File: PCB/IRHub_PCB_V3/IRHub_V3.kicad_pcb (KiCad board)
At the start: 2 copper layers, 80 x 80 mm, 85 parts, among them Q1 UMH3N, SW1 SW_Push, U1 DRV2605LDGS

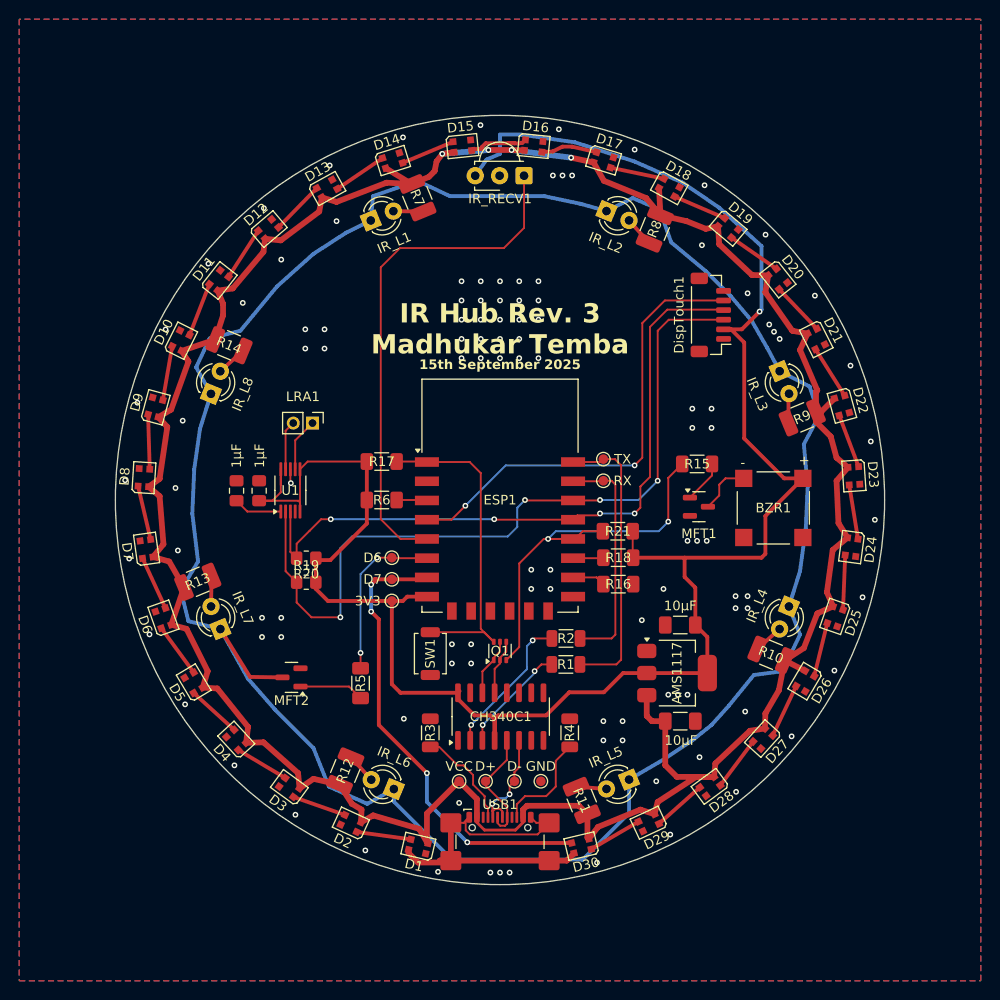
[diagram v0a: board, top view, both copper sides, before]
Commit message: fix pcb led issue :)
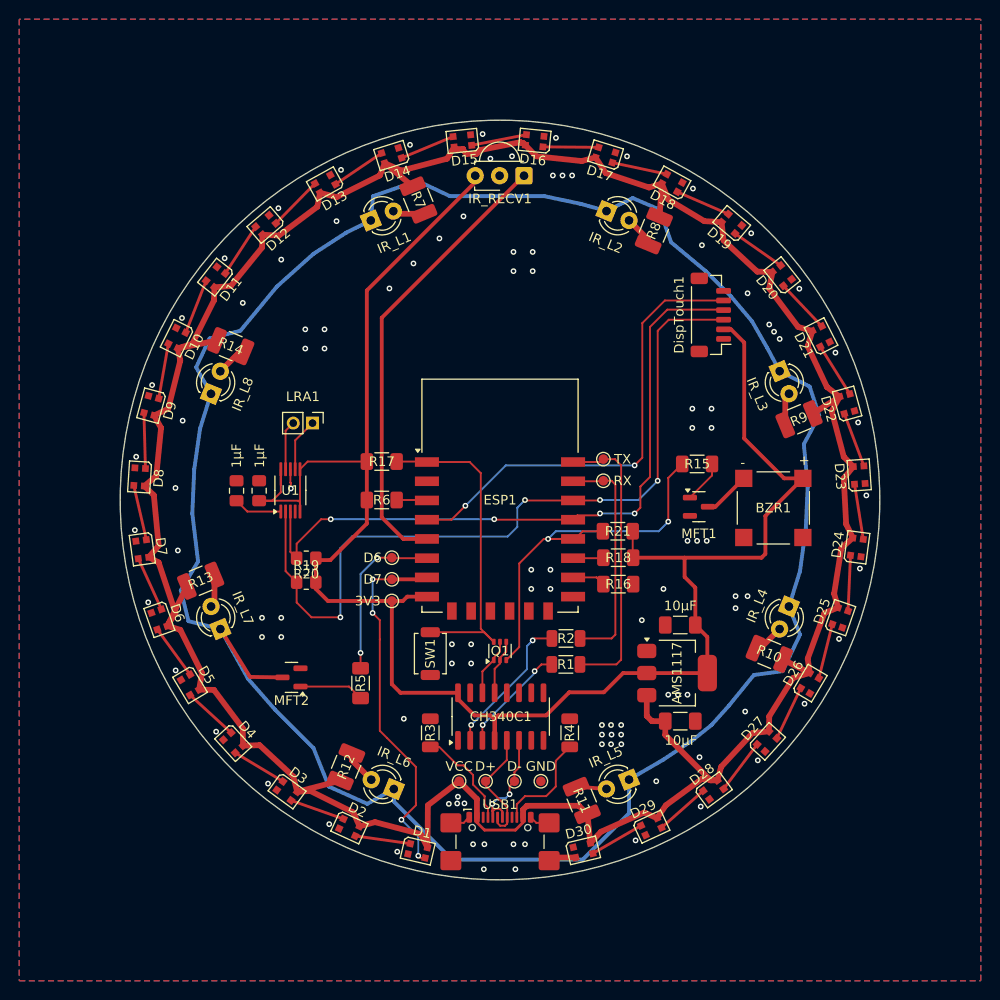
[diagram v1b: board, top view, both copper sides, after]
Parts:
- moved D20 0.57 mm to (179.3, 76.7), turned to 128.4 degrees
- moved D21 0.57 mm to (183.4, 83.0), turned to 116.9 degrees
- moved D19 0.57 mm to (174.1, 71.3), turned to 139.9 degrees
- moved D22 0.56 mm to (186.1, 90.0), turned to 105.4 degrees
- moved D18 0.56 mm to (167.9, 67.0), turned to 151.4 degrees
- moved D23 0.56 mm to (187.4, 97.4), turned to 93.9 degrees
- moved D17 0.56 mm to (161.0, 64.1), turned to 162.9 degrees
- moved D24 0.55 mm to (187.1, 104.9), turned to 82.4 degrees
- moved D16 0.55 mm to (153.6, 62.6), turned to 174.4 degrees
- moved D25 0.54 mm to (185.4, 112.2), turned to 70.9 degrees
- moved D15 0.54 mm to (146.1, 62.7), turned to -174.1 degrees
- moved D26 0.53 mm to (182.2, 119.0), turned to 59.4 degrees
- moved D14 0.53 mm to (138.7, 64.2), turned to -162.6 degrees
- moved D27 0.52 mm to (177.8, 125.1), turned to 47.9 degrees
- moved D13 0.52 mm to (131.8, 67.1), turned to -151.1 degrees
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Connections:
- D1 pad 1: unconnected-(D1-DOUT-Pad1) -> Net-(D1-DOUT)
- D1 pad 2: +5V -> GND
- D1 pad 3: Net-(D1-DIN) -> D7
- D1 pad 4: GND -> +5V
- D10 pad 2: +5V -> GND
- D10 pad 4: GND -> +5V
- D11 pad 1: Net-(D10-DIN) -> Net-(D11-DOUT)
- D11 pad 2: +5V -> GND
- D11 pad 3: Net-(D11-DIN) -> Net-(D10-DOUT)
- D11 pad 4: GND -> +5V
- D12 pad 1: Net-(D11-DIN) -> Net-(D12-DOUT)
- D12 pad 2: +5V -> GND
- D12 pad 3: Net-(D12-DIN) -> Net-(D11-DOUT)
- D12 pad 4: GND -> +5V
- D13 pad 1: Net-(D12-DIN) -> Net-(D13-DOUT)
- D13 pad 2: +5V -> GND
- D13 pad 3: Net-(D13-DIN) -> Net-(D12-DOUT)
- D13 pad 4: GND -> +5V
- D14 pad 1: Net-(D13-DIN) -> Net-(D14-DOUT)
- D14 pad 2: +5V -> GND
- D14 pad 3: Net-(D14-DIN) -> Net-(D13-DOUT)
- D14 pad 4: GND -> +5V
- D15 pad 1: Net-(D14-DIN) -> Net-(D15-DOUT)
- D15 pad 2: +5V -> GND
- D15 pad 3: Net-(D15-DIN) -> Net-(D14-DOUT)
- D15 pad 4: GND -> +5V
- D16 pad 1: Net-(D15-DIN) -> Net-(D16-DOUT)
- D16 pad 2: +5V -> GND
- D16 pad 3: Net-(D16-DIN) -> Net-(D15-DOUT)
- D16 pad 4: GND -> +5V
- D17 pad 1: Net-(D16-DIN) -> Net-(D17-DOUT)
- D17 pad 2: +5V -> GND
- D17 pad 3: Net-(D17-DIN) -> Net-(D16-DOUT)
- D17 pad 4: GND -> +5V
- D18 pad 1: Net-(D17-DIN) -> Net-(D18-DOUT)
- D18 pad 2: +5V -> GND
- D18 pad 3: Net-(D18-DIN) -> Net-(D17-DOUT)
- D18 pad 4: GND -> +5V
- D19 pad 1: Net-(D18-DIN) -> Net-(D19-DOUT)
- D19 pad 2: +5V -> GND
- D19 pad 3: Net-(D19-DIN) -> Net-(D18-DOUT)
- D19 pad 4: GND -> +5V
- D2 pad 1: Net-(D1-DIN) -> Net-(D2-DOUT)
- D2 pad 2: +5V -> GND
- D2 pad 3: Net-(D2-DIN) -> Net-(D1-DOUT)
- D2 pad 4: GND -> +5V
- D20 pad 1: Net-(D19-DIN) -> Net-(D20-DOUT)
- D20 pad 2: +5V -> GND
- D20 pad 3: Net-(D20-DIN) -> Net-(D19-DOUT)
- D20 pad 4: GND -> +5V
- D21 pad 1: Net-(D20-DIN) -> Net-(D21-DOUT)
- D21 pad 2: +5V -> GND
- D21 pad 3: Net-(D21-DIN) -> Net-(D20-DOUT)
- D21 pad 4: GND -> +5V
- D22 pad 1: Net-(D21-DIN) -> Net-(D22-DOUT)
- D22 pad 2: +5V -> GND
- D22 pad 3: Net-(D22-DIN) -> Net-(D21-DOUT)
- D22 pad 4: GND -> +5V
- D23 pad 1: Net-(D22-DIN) -> Net-(D23-DOUT)
- D23 pad 2: +5V -> GND
- D23 pad 3: Net-(D23-DIN) -> Net-(D22-DOUT)
- D23 pad 4: GND -> +5V
- D24 pad 1: Net-(D23-DIN) -> Net-(D24-DOUT)
- D24 pad 2: +5V -> GND
- D24 pad 3: Net-(D24-DIN) -> Net-(D23-DOUT)
- D24 pad 4: GND -> +5V
- D25 pad 1: Net-(D24-DIN) -> Net-(D25-DOUT)
- D25 pad 2: +5V -> GND
- D25 pad 3: Net-(D25-DIN) -> Net-(D24-DOUT)
- D25 pad 4: GND -> +5V
- D26 pad 1: Net-(D25-DIN) -> Net-(D26-DOUT)
- D26 pad 2: +5V -> GND
- D26 pad 3: Net-(D26-DIN) -> Net-(D25-DOUT)
- D26 pad 4: GND -> +5V
- D27 pad 1: Net-(D26-DIN) -> Net-(D27-DOUT)
- D27 pad 2: +5V -> GND
- D27 pad 3: Net-(D27-DIN) -> Net-(D26-DOUT)
- D27 pad 4: GND -> +5V
- D28 pad 1: Net-(D27-DIN) -> Net-(D28-DOUT)
- D28 pad 2: +5V -> GND
- D28 pad 3: Net-(D28-DIN) -> Net-(D27-DOUT)
- D28 pad 4: GND -> +5V
- D29 pad 1: Net-(D28-DIN) -> Net-(D29-DOUT)
- D29 pad 2: +5V -> GND
- D29 pad 3: Net-(D29-DIN) -> Net-(D28-DOUT)
- D29 pad 4: GND -> +5V
- D3 pad 1: Net-(D2-DIN) -> Net-(D3-DOUT)
- D3 pad 2: +5V -> GND
- D3 pad 3: Net-(D3-DIN) -> Net-(D2-DOUT)
- D3 pad 4: GND -> +5V
- D30 pad 1: Net-(D29-DIN) -> unconnected-(D30-DOUT-Pad1)
- D30 pad 2: +5V -> GND
- D30 pad 3: D7 -> Net-(D29-DOUT)
- D30 pad 4: GND -> +5V
- D4 pad 1: Net-(D3-DIN) -> Net-(D4-DOUT)
- D4 pad 2: +5V -> GND
- D4 pad 3: Net-(D4-DIN) -> Net-(D3-DOUT)
- D4 pad 4: GND -> +5V
- D5 pad 1: Net-(D4-DIN) -> Net-(D5-DOUT)
- D5 pad 2: +5V -> GND
- D5 pad 3: Net-(D5-DIN) -> Net-(D4-DOUT)
- D5 pad 4: GND -> +5V
- D6 pad 1: Net-(D5-DIN) -> Net-(D6-DOUT)
- D6 pad 2: +5V -> GND
- D6 pad 3: Net-(D6-DIN) -> Net-(D5-DOUT)
- D6 pad 4: GND -> +5V
- D7 pad 1: Net-(D6-DIN) -> Net-(D7-DOUT)
- D7 pad 2: +5V -> GND
- D7 pad 3: Net-(D7-DIN) -> Net-(D6-DOUT)
- D7 pad 4: GND -> +5V
- D8 pad 1: Net-(D7-DIN) -> Net-(D8-DOUT)
- D8 pad 2: +5V -> GND
- D8 pad 3: Net-(D8-DIN) -> Net-(D7-DOUT)
- D8 pad 4: GND -> +5V
- D9 pad 1: Net-(D8-DIN) -> Net-(D10-DIN)
- D9 pad 2: +5V -> GND
- D9 pad 3: Net-(D10-DOUT) -> Net-(D8-DOUT)
- D9 pad 4: GND -> +5V
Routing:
- net GND: track 41.2 -> 10.0 mm, vias 113 -> 108
- net +3.3V: track 209.8 -> 195.9 mm, vias 1 -> 0
- net +5V: track 292.0 -> 305.5 mm, vias 4 -> 0
- net D7: track 48.1 -> 38.5 mm
- net D5: track 53.9 -> 47.3 mm
- net Net-(D15-DIN): track 6.18 -> 0.00 mm
- net Net-(D16-DIN): track 5.89 -> 0.00 mm
- net Net-(D6-DOUT): track 0.00 -> 5.80 mm
- net Net-(D28-DOUT): track 0.00 -> 5.80 mm
- net Net-(D23-DOUT): track 0.00 -> 5.80 mm
- net Net-(D17-DOUT): track 0.00 -> 5.80 mm
- net Net-(D1-DOUT): track 0.00 -> 5.80 mm
- net Net-(D7-DOUT): track 0.00 -> 5.80 mm
- net Net-(D4-DOUT): track 0.00 -> 5.80 mm
- net Net-(D27-DOUT): track 0.00 -> 5.80 mm
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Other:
- board size 80 x 80 mm -> 79 x 79 mm
- board text removed: "15th September 2025"
- board text removed: "IR Hub Rev. 3 Madhukar Temba"

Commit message: new pcb
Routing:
- net D7: track 38.5 -> 39.2 mm
- net D6: track 17.4 -> 18.1 mm
- net GND: vias 108 -> 112
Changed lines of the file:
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@@
 	)
 	(via
+		(at 153.2 77.2)
+		(size 0.6)
+		(drill 0.3)
+		(layers "F.Cu" "B.Cu")
+		(free yes)
+		(net 2)
+	)
+	(via
 		(at 140 122.75)
 		(size 0.6)
@@
 	)
 	(via
-		(at 151.4 74.2)
+		(at 147.2 77.2)
+		(size 0.6)
+		(drill 0.3)
+		(layers "F.Cu" "B.Cu")
+		(free yes)
+		(net 2)
+	)
+	(via
+		(at 151.2 77.2)
 		(size 0.6)
 		(drill 0.3)
@@
 	)
 	(via
-		(at 151.4 76.2)
+		(at 147.2 79.2)
 		(size 0.6)
 		(drill 0.3)
@@
 	)
 	(via
+		(at 153.2 79.2)
+		(size 0.6)
+		(drill 0.3)
+		(layers "F.Cu" "B.Cu")
+		(free yes)
+		(net 2)
+	)
+	(via
 		(at 149 64.5)
 		(size 0.6)
@@
 	)
 	(via
-		(at 153.4 74.2)
+		(at 149.2 77.2)
 		(size 0.6)
 		(drill 0.3)
@@
 	)
 	(via
-		(at 153.4 76.2)
+		(at 149.2 79.2)
 		(size 0.6)
 		(drill 0.3)
@@
 	)
 	(via
+		(at 151.2 79.2)
+		(size 0.6)
+		(drill 0.3)
+		(layers "F.Cu" "B.Cu")
+		(free yes)
+		(net 2)
+	)
+	(via
 		(at 155.5 66.25)
 		(size 0.6)
@@
 	)
 	(segment
-		(start 141.726358 137.226358)
-		(end 141.5 137)
-		(width 0.2)
+		(start 141.2 131)
+		(end 141.2 127.8)
+		(width 0.4)
 		(layer "F.Cu")
 		(net 47)
 	)
 	(segment
-		(start 137.5 124)
-		(end 137.5 114.5)
-		(width 0.2)
+		(start 141.5 136.5)
+		(end 141.586019 136.586019)
+		(width 0.4)
 		(layer "F.Cu")
 		(net 47)
 	)
 	(segment
-		(start 141.25 131.5)
-		(end 141.25 127.75)
-		(width 0.2)
+		(start 141.586019 136.586019)
+		(end 141.586019 136.6)
+		(width 0.4)
 		(layer "F.Cu")
 		(net 47)
 	)
 	(segment
-		(start 139.75 133.25)
-		(end 141.25 131.75)
-		(width 0.2)
+		(start 141.586019 136.6)
+		(end 142.212377 137.226358)
+		(width 0.4)
 		(layer "F.Cu")
 		(net 47)
 	)
 	(segment
-		(start 136.75 108.25)
-		(end 138.75 108.25)
-		(width 0.2)
+		(start 138.75 108.25)
+		(end 136.75 108.25)
+		(width 0.4)
 		(layer "F.Cu")
 		(net 47)
@@
 	)
 	(segment
-		(start 138.25 124.75)
-		(end 137.5 124)
-		(width 0.2)
-		(layer "F.Cu")
-		(net 47)
-	)
-	(segment
-		(start 141.25 127.75)
-		(end 138.25 124.75)
-		(width 0.2)
+		(start 139.1 133.1)
+		(end 141.2 131)
+		(width 0.4)
 		(layer "F.Cu")
 		(net 47)
 	)
 	(segment
-		(start 141.25 131.75)
-		(end 141.25 131.5)
-		(width 0.2)
+		(start 137.4 112.4)
+		(end 136.8 111.8)
+		(width 0.4)
 		(layer "F.Cu")
 		(net 47)
 	)
 	(segment
-		(start 142.212377 137.226358)
-		(end 141.726358 137.226358)
-		(width 0.2)
+		(start 141.2 127.8)
+		(end 137.4 124)
+		(width 0.4)
 		(layer "F.Cu")
 		(net 47)
 	)
 	(segment
-		(start 137.5 112.5)
-		(end 136.75 111.75)
-		(width 0.2)
+		(start 136.75 108.25)
+		(end 136.6 108.4)
+		(width 0.4)
 		(layer "F.Cu")
 		(net 47)
 	)
 	(segment
-		(start 137.5 114.5)
-		(end 137.5 112.5)
-		(width 0.2)
+		(start 138.75 108.25)
+		(end 142.2 108.25)
+		(width 0.4)
 		(layer "F.Cu")
 		(net 47)
 	)
 	(segment
-		(start 138.75 108.25)
-		(end 142.2 108.25)
+		(start 137.4 124)
+		(end 137.4 112.4)
 		(width 0.4)
 		(layer "F.Cu")
@@
 	)
 	(via
-		(at 136.75 108.25)
+		(at 141.5 136.5)
 		(size 0.6)
 		(drill 0.3)
@@
 	)
 	(via
-		(at 141.5 137)
+		(at 136.8 111.8)
 		(size 0.6)
 		(drill 0.3)
@@
 	)
 	(via
-		(at 136.75 111.75)
+		(at 136.6 108.4)
 		(size 0.6)
 		(drill 0.3)
@@
 	)
 	(via
-		(at 139.75 133.25)
+		(at 139.1 133.1)
 		(size 0.6)
 		(drill 0.3)
@@
 	)
 	(segment
-		(start 141.5 137)
-		(end 141.5 135)
-		(width 0.2)
+		(start 139.1 133.1)
+		(end 139.4 133.4)
+		(width 0.4)
 		(layer "B.Cu")
 		(net 47)
 	)
 	(segment
-		(start 141.5 135)
-		(end 139.75 133.25)
-		(width 0.2)
+		(start 140 133.4)
+		(end 141.4 134.8)
+		(width 0.4)
 		(layer "B.Cu")
 		(net 47)
 	)
 	(segment
-		(start 136.75 111.75)
-		(end 136.75 108.25)
-		(width 0.2)
+		(start 141.4 136.4)
+		(end 141.5 136.5)
+		(width 0.4)
+		(layer "B.Cu")
+		(net 47)
+	)
+	(segment
+		(start 141.4 134.8)
+		(end 141.4 136.4)
+		(width 0.4)
+		(layer "B.Cu")
+		(net 47)
+	)
+	(segment
+		(start 136.6 108.4)
+		(end 136.6 111.6)
+		(width 0.4)
+		(layer "B.Cu")
+		(net 47)
+	)
+	(segment
+		(start 136.6 111.6)
+		(end 136.8 111.8)
+		(width 0.4)
+		(layer "B.Cu")
+		(net 47)
+	)
+	(segment
+		(start 139.4 133.4)
+		(end 140 133.4)
+		(width 0.4)
 		(layer "B.Cu")
 		(net 47)
@@
 		(start 142.4 106.05)
 		(end 138.8 106.05)
-		(width 0.2)
+		(width 0.4)
 		(layer "F.Cu")
 		(net 55)
 	)
 	(segment
-		(start 135.5 115.9)
-		(end 135.5 117.5)
-		(width 0.2)
+		(start 138.75 106)
+		(end 136.2 106)
+		(width 0.4)
 		(layer "F.Cu")
 		(net 55)
 	)
 	(segment
-		(start 138.75 106)
-		(end 137.2 106)
-		(width 0.2)
+		(start 135.4 117.4)
+		(end 135.5 117.5)
+		(width 0.4)
 		(layer "F.Cu")
 		(net 55)
@@
 		(start 138.8 106.05)
 		(end 138.75 106)
-		(width 0.2)
+		(width 0.4)
+		(layer "F.Cu")
+		(net 55)
+	)
+	(segment
+		(start 136.2 106)
+		(end 135.4 106.8)
+		(width 0.4)
+		(layer "F.Cu")
+		(net 55)
+	)
+	(segment
+		(start 135.4 115.2)
+		(end 135.4 117.4)
+		(width 0.4)
 		(layer "F.Cu")
 		(net 55)
 	)
 	(via
-		(at 135.5 115.9)
+		(at 135.4 115.2)
 		(size 0.6)
 		(drill 0.3)
@@
 	)
 	(via
-		(at 137.2 106)
+		(at 135.4 106.8)
 		(size 0.6)
 		(drill 0.3)
@@
 	)
 	(segment
-		(start 135.5 107.7)
-		(end 137.2 106)
-		(width 0.2)
-		(layer "B.Cu")
-		(net 55)
-	)
-	(segment
-		(start 135.5 115.9)
-		(end 135.5 107.7)
-		(width 0.2)
+		(start 135.4 106.8)
+		(end 135.4 115.2)
+		(width 0.4)
 		(layer "B.Cu")
 		(net 55)
@@
 		(start 129.25 119.4)
 		(end 134.3 119.4)
-		(width 0.2)
+		(width 0.4)
 		(layer "F.Cu")
 		(net 77)
@@
 		(start 134.3 119.4)
 		(end 135.5 120.6)
-		(width 0.2)
+		(width 0.4)
 		(layer "F.Cu")
 		(net 77)

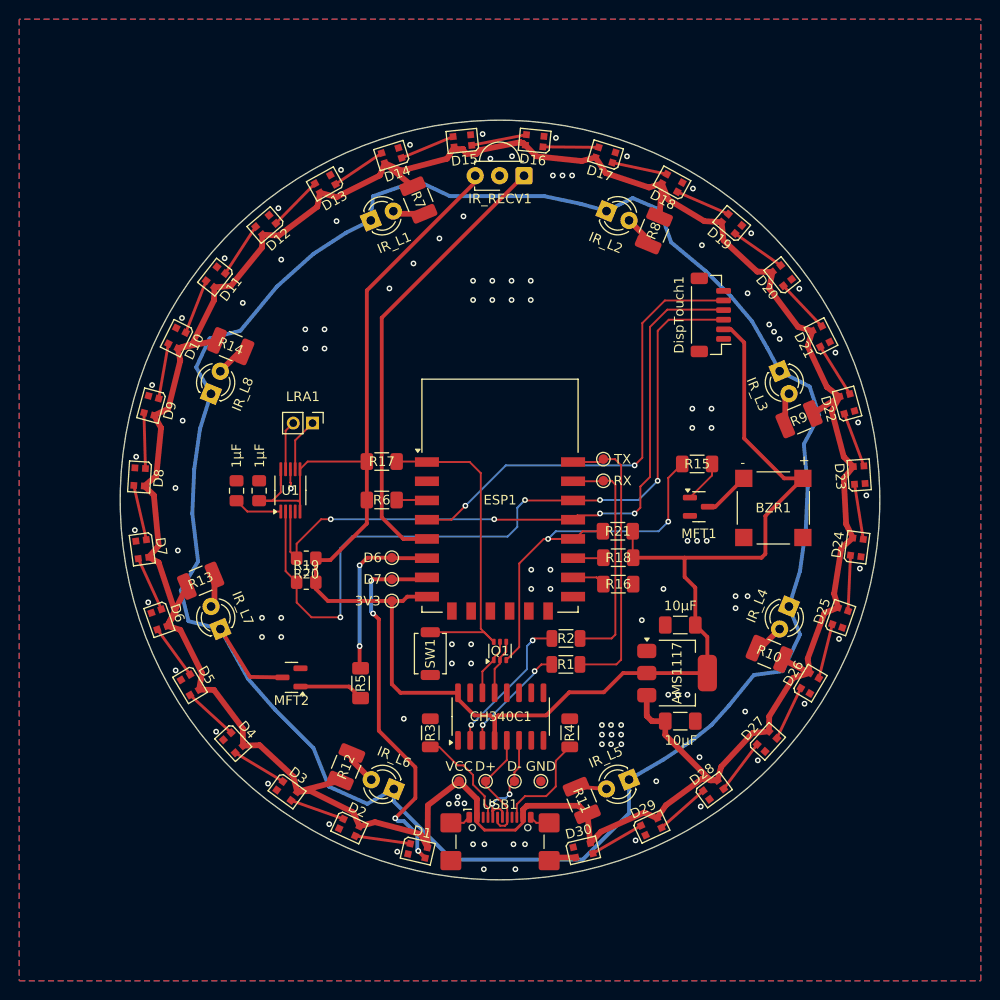
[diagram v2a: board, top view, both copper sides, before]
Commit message: add vias
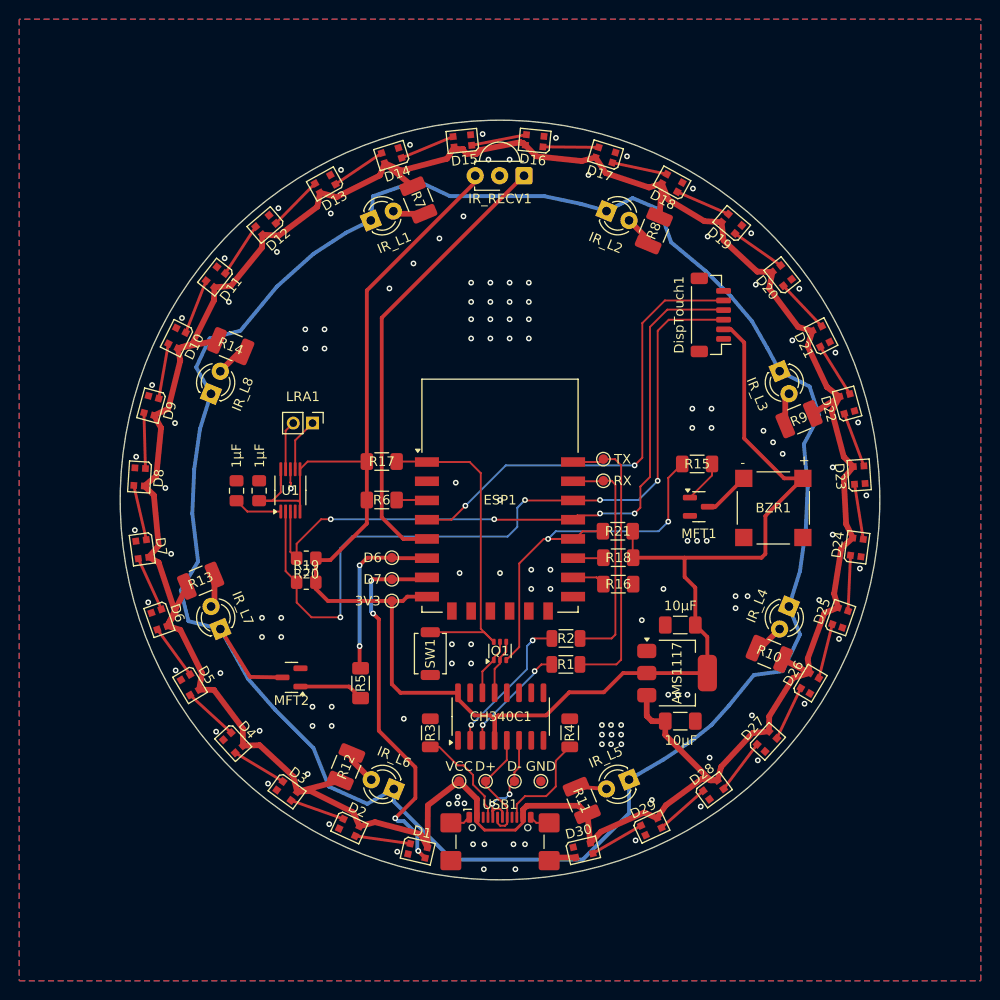
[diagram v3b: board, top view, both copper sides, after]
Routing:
- net GND: vias 112 -> 133

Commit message: small space savings for the oled conn
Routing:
- net D5: track 47.3 -> 57.0 mm, vias 0 -> 2
- net +3.3V: track 195.9 -> 202.4 mm, vias 0 -> 2
- net GND: vias 133 -> 130

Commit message: new updated version with oled connector
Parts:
- added C10: 2µF, Capacitor_SMD:C_0805_2012Metric_Pad1.18x1.45mm_HandSolder, F.Cu at (136.6, 81.8)
- added C11: 0.1µF, Capacitor_SMD:C_0805_2012Metric_Pad1.18x1.45mm_HandSolder, F.Cu at (136.6, 78.8)
- added C5: 1µF, Capacitor_SMD:C_0805_2012Metric_Pad1.18x1.45mm_HandSolder, F.Cu at (159.8, 75.6)
- added C6: 1µF, Capacitor_SMD:C_0805_2012Metric_Pad1.18x1.45mm_HandSolder, F.Cu at (157.2, 75.6)
- added C7: 1µF, Capacitor_SMD:C_0805_2012Metric_Pad1.18x1.45mm_HandSolder, F.Cu at (140.2, 75.6)
- added C8: 10µF, Capacitor_SMD:C_0805_2012Metric_Pad1.18x1.45mm_HandSolder, F.Cu at (153.6, 75.6)
- added C9: 0.1µF, Capacitor_SMD:C_0805_2012Metric_Pad1.18x1.45mm_HandSolder, F.Cu at (136.6, 84.8)
- added DS1: OLED-128O064D, Display:OLED-128O064D, F.Cu at (150.0, 79.8)
- added R22: 10000, Resistor_SMD:R_0805_2012Metric_Pad1.20x1.40mm_HandSolder, F.Cu at (149.6, 75.6)
- added R23: 10000, Resistor_SMD:R_0805_2012Metric_Pad1.20x1.40mm_HandSolder, F.Cu at (147.6, 75.6)
- added R24: 390000, Resistor_SMD:R_0805_2012Metric_Pad1.20x1.40mm_HandSolder, F.Cu at (142.2, 75.6)
- added R25: 10000, Resistor_SMD:R_0805_2012Metric_Pad1.20x1.40mm_HandSolder, F.Cu at (151.6, 75.6)
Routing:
- net +3.3V: track 202.4 -> 263.2 mm
- net GND: track 10.0 -> 43.1 mm, vias 130 -> 134
- net D2: track 71.6 -> 99.3 mm, vias 4 -> 6
- net D1: track 82.4 -> 108.7 mm, vias 4 -> 6
- net Net-(DS1-C1N): track 0.00 -> 6.10 mm
- net Net-(DS1-C2P): track 0.00 -> 5.63 mm
- net Net-(DS1-~{RES}): track 0.00 -> 5.40 mm
- net Net-(DS1-VCOMH): track 0.00 -> 3.84 mm
- net Net-(DS1-C1P): track 0.00 -> 3.47 mm
- net Net-(DS1-IREF): track 0.00 -> 3.34 mm
- net Net-(DS1-C2N): track 0.00 -> 3.26 mm
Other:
- board text added: "23rd September 2025"
- board text added: "IR Hub Rev. 3"
- board text added: "JLCJLCJLCJLC"
- board text added: "LRA"
- board text added: "Madhukar Temba"

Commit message: final production build, hope I didn't mess something up this time :)
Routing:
- net GND: vias 134 -> 133
